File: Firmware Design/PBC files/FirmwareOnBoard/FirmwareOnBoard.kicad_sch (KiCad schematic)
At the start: 70 parts, among them J1 Conn_ST_STDC14, J2 USB_C_Receptacle_USB2.0_16P, J3 Barrel_Jack_Switch, J4 NRF24L01 + PA/LNA, J5 OLED HS91L02W2C01, J6 Conn_01x04_Pin, SW1 SW_Push, SW2 SW_Push, SW3 KMR223G LFG, SW4 SW_Push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

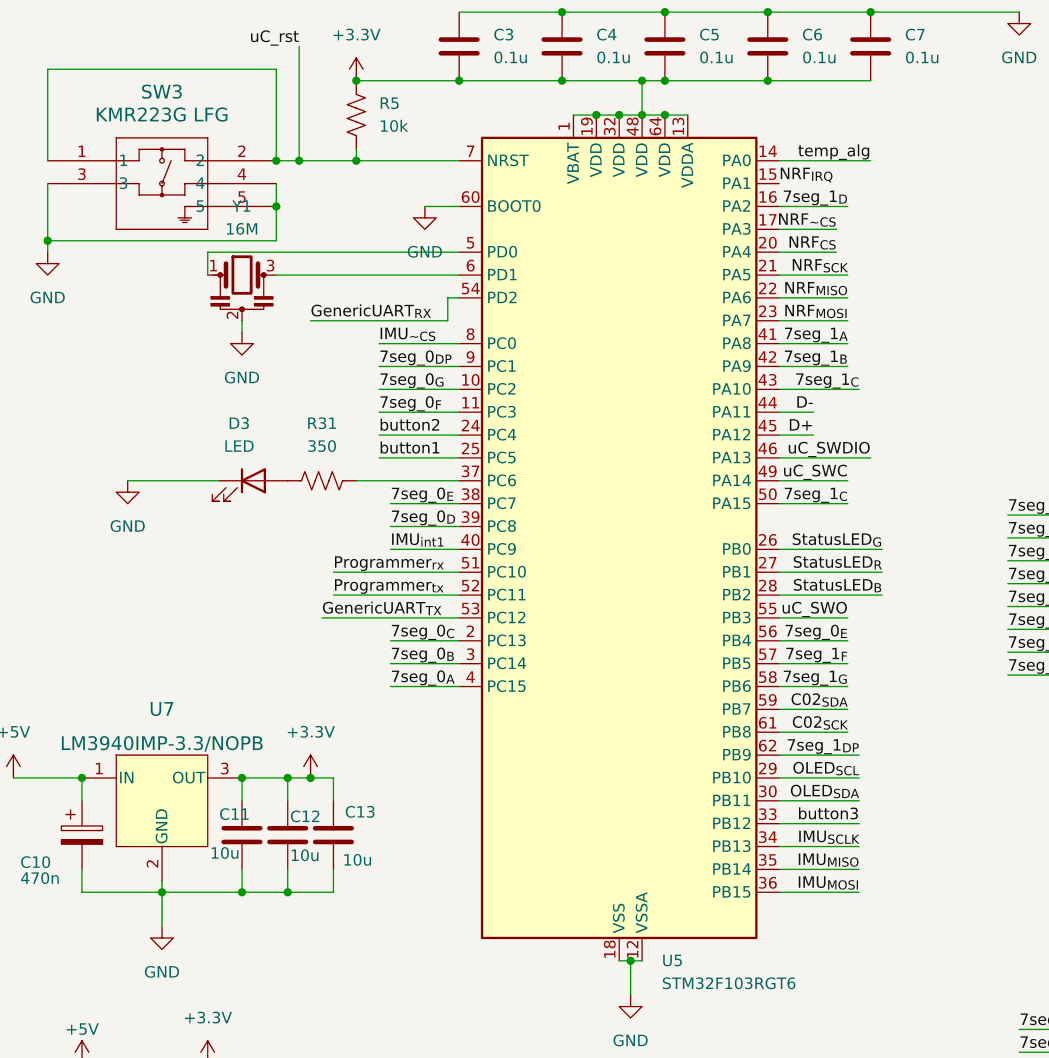
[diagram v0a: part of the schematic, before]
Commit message: Complete first draft of layout placement
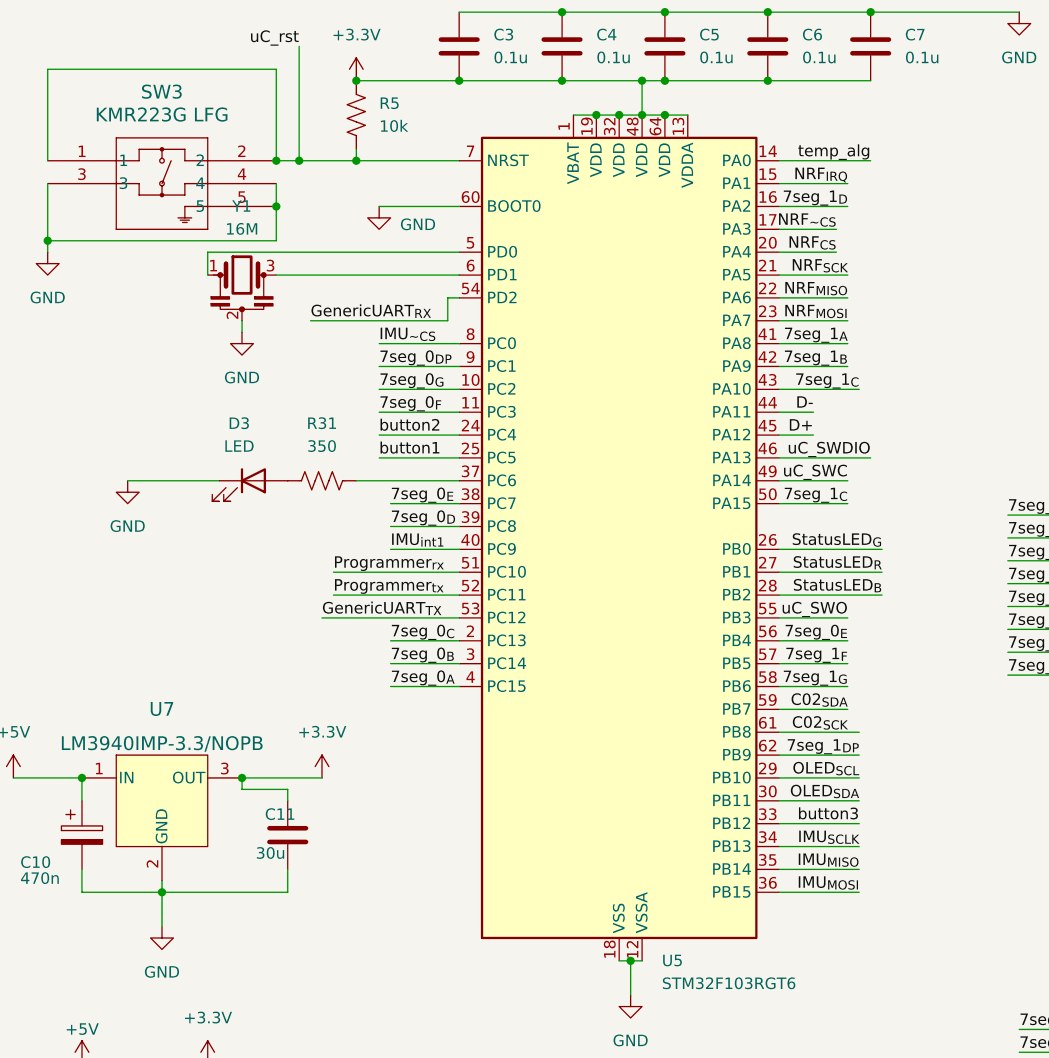
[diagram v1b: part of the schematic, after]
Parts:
- removed C12, C13: 10u, Capacitor_SMD:C_0603_1608Metric, symbol Device:C
- C1, C2, C3, C4, C5, C6, C7, C8, C9: footprint (none) -> Capacitor_SMD:C_0603_1608Metric
- C11: value 10u -> 30u
- D1: footprint (none) -> Diode_THT:D_DO-15_P12.70mm_Horizontal
- D3: footprint (none) -> LED_SMD:LED_0805_2012Metric
- J2: footprint (none) -> Connector_USB:USB_C_Receptacle_HRO_TYPE-C-31-M-12
- J5: footprint (none) -> Connector_PinHeader_2.54mm:PinHeader_1x04_P2.54mm_Vertical
- J6: footprint (none) -> TerminalBlock:TerminalBlock_Altech_AK300-4_P5.00mm
- L1: footprint (none) -> Inductor_SMD:L_0201_0603Metric
- R12, R13, R14, R15, R16, R17, R18, R19, R20, R21, R22, R23, R24, R25, R26, R27, R28, R29, R30, R5: footprint (none) -> Resistor_SMD:R_0603_1608Metric
- SW1, SW2, SW4: footprint (none) -> Buttons_Switches_Keyboard.pretty-master:SW_Cherry_MX1A_1.00u_PCB
- SW3: footprint flight_stick_footprints:KMR2_G_CNK -> old flightstick footpritns:KMR2_G_CNK
- U6, U8: footprint Display_7Segment:HDSP-7401 -> old flightstick footpritns:HDSP-7401NEWADJUSETED
- U7: footprint flight_stick_footprints:MP04A -> old flightstick footpritns:MP04A
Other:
- moved on the sheet: C11
